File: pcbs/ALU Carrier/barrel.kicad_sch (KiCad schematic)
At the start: 3 parts, among them U6001 74HC14

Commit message: Working towards the connectors
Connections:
- net B3: now also U6001.13; no longer U6001.1
- net B3_inv: now also U6001.12; no longer U6001.2
- net GND: now also U6001.1; no longer U6001.13
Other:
- moved on the sheet: U6001A, U6001F
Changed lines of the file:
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@@
 	(symbol
 		(lib_id "74xx:74HC14")
-		(at 83.82 177.8 0)
+		(at 83.82 114.3 0)
 		(unit 6)
 		(exclude_from_sim no)
@@
 		(fields_autoplaced yes)
 		(property "Reference" "U6001"
-			(at 83.82 168.91 0)
+			(at 83.82 105.41 0)
 			(effects
 				(font
@@
 		)
 		(property "Value" "74HC14"
-			(at 83.82 171.45 0)
+			(at 83.82 107.95 0)
 			(effects
 				(font
@@
 		)
 		(property "Footprint" "Package_SO:SOIC-14_3.9x8.7mm_P1.27mm"
-			(at 83.82 177.8 0)
+			(at 83.82 114.3 0)
 			(effects
 				(font
@@
 		)
 		(property "Datasheet" "https://www.lcsc.com/datasheet/lcsc_datasheet_2407241044_Nexperia-74HC14D-653_C5605.pdf"
-			(at 83.82 177.8 0)
+			(at 83.82 114.3 0)
 			(effects
 				(font
@@
 		)
 		(property "Description" "Hex inverter schmitt trigger"
-			(at 83.82 177.8 0)
+			(at 83.82 114.3 0)
 			(effects
 				(font
@@
 		)
 		(property "LCSC" "C5605"
-			(at 83.82 177.8 0)
+			(at 83.82 114.3 0)
 			(effects
 				(font
@@
 	(symbol
 		(lib_id "74xx:74HC14")
-		(at 83.82 114.3 0)
+		(at 83.82 177.8 0)
 		(unit 1)
 		(exclude_from_sim no)
@@
 		(fields_autoplaced yes)
 		(property "Reference" "U6001"
-			(at 83.82 105.41 0)
+			(at 83.82 168.91 0)
 			(effects
 				(font
@@
 		)
 		(property "Value" "74HC14"
-			(at 83.82 107.95 0)
+			(at 83.82 171.45 0)
 			(effects
 				(font
@@
 		)
 		(property "Footprint" "Package_SO:SOIC-14_3.9x8.7mm_P1.27mm"
-			(at 83.82 114.3 0)
+			(at 83.82 177.8 0)
 			(effects
 				(font
@@
 		)
 		(property "Datasheet" "https://www.lcsc.com/datasheet/lcsc_datasheet_2407241044_Nexperia-74HC14D-653_C5605.pdf"
-			(at 83.82 114.3 0)
+			(at 83.82 177.8 0)
 			(effects
 				(font
@@
 		)
 		(property "Description" "Hex inverter schmitt trigger"
-			(at 83.82 114.3 0)
+			(at 83.82 177.8 0)
 			(effects
 				(font
@@
 		)
 		(property "LCSC" "C5605"
-			(at 83.82 114.3 0)
-			(effects
-				(font
+			(at 83.82 177.8 0)
+			(effects
+				(font

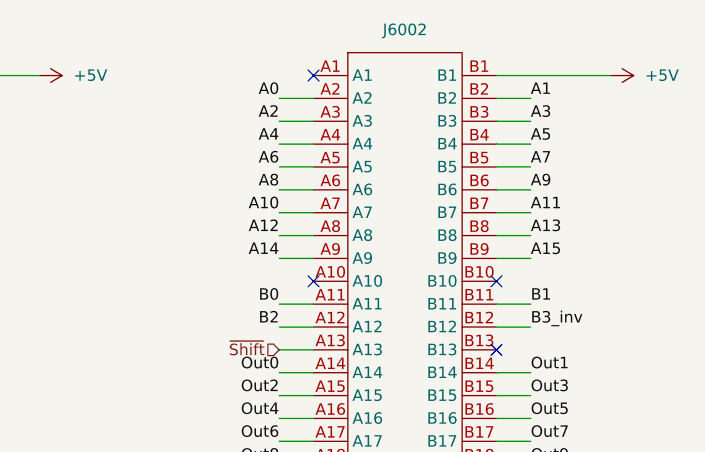
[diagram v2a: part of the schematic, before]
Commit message: Correcting barrel shifter
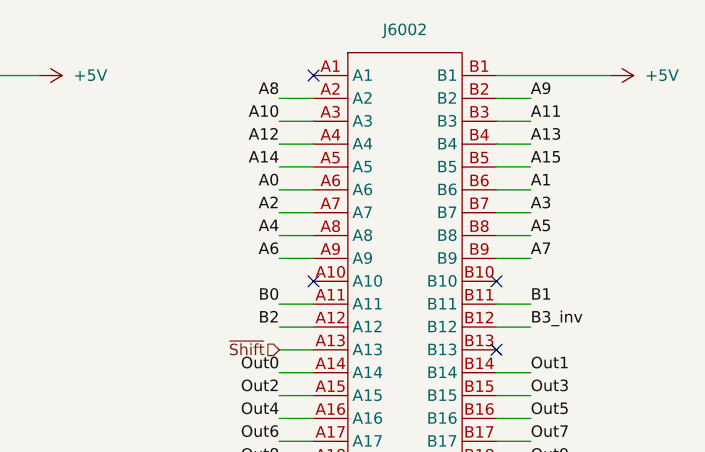
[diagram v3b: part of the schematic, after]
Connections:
- net A0: now also J6002.A6; no longer J6002.A2
- net A1: now also J6002.B6; no longer J6002.B2
- net A10: now also J6002.A3; no longer J6002.A7
- net A11: now also J6002.B3; no longer J6002.B7
- net A12: now also J6002.A4; no longer J6002.A8
- net A13: now also J6002.B4; no longer J6002.B8
- net A14: now also J6002.A5; no longer J6002.A9
- net A15: now also J6002.B5; no longer J6002.B9
- net A2: now also J6002.A7; no longer J6002.A3
- net A3: now also J6002.B7; no longer J6002.B3
- net A4: now also J6002.A8; no longer J6002.A4
- net A5: now also J6002.B8; no longer J6002.B4
- net A6: now also J6002.A9; no longer J6002.A5
- net A7: now also J6002.B9; no longer J6002.B5
- net A8: now also J6002.A2; no longer J6002.A6
- net A9: now also J6002.B2; no longer J6002.B6
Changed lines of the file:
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@@
 	)
 	(label "A4"
-		(at 179.07 43.18 180)
+		(at 179.07 53.34 180)
 		(fields_autoplaced yes)
 		(effects
@@
 	)
 	(label "A10"
-		(at 179.07 50.8 180)
+		(at 179.07 40.64 180)
 		(fields_autoplaced yes)
 		(effects
@@
 	)
 	(label "A11"
-		(at 207.01 50.8 0)
+		(at 207.01 40.64 0)
 		(fields_autoplaced yes)
 		(effects
@@
 	)
 	(label "A2"
-		(at 179.07 40.64 180)
+		(at 179.07 50.8 180)
 		(fields_autoplaced yes)
 		(effects
@@
 	)
 	(label "A8"
-		(at 179.07 48.26 180)
+		(at 179.07 38.1 180)
 		(fields_autoplaced yes)
 		(effects
@@
 	)
 	(label "A6"
-		(at 179.07 45.72 180)
+		(at 179.07 55.88 180)
 		(fields_autoplaced yes)
 		(effects
@@
 	)
 	(label "A0"
-		(at 179.07 38.1 180)
+		(at 179.07 48.26 180)
 		(fields_autoplaced yes)
 		(effects
@@
 	)
 	(label "A7"
-		(at 207.01 45.72 0)
+		(at 207.01 55.88 0)
 		(fields_autoplaced yes)
 		(effects
@@
 	)
 	(label "A3"
-		(at 207.01 40.64 0)
+		(at 207.01 50.8 0)
 		(fields_autoplaced yes)
 		(effects
@@
 	)
 	(label "A12"
-		(at 179.07 53.34 180)
+		(at 179.07 43.18 180)
 		(fields_autoplaced yes)
 		(effects
@@
 	)
 	(label "A5"
-		(at 207.01 43.18 0)
+		(at 207.01 53.34 0)
 		(fields_autoplaced yes)
 		(effects
@@
 	)
 	(label "A14"
-		(at 179.07 55.88 180)
+		(at 179.07 45.72 180)
 		(fields_autoplaced yes)
 		(effects
@@
 	)
 	(label "A15"
-		(at 207.01 55.88 0)
+		(at 207.01 45.72 0)
 		(fields_autoplaced yes)
 		(effects
@@
 	)
 	(label "A1"
-		(at 207.01 38.1 0)
+		(at 207.01 48.26 0)
 		(fields_autoplaced yes)
 		(effects
@@
 	)
 	(label "A9"
-		(at 207.01 48.26 0)
+		(at 207.01 38.1 0)
 		(fields_autoplaced yes)
 		(effects
@@
 	)
 	(label "A13"
-		(at 207.01 53.34 0)
-		(fields_autoplaced yes)
-		(effects
+		(at 207.01 43.18 0)
+		(fields_autoplaced yes)
+		(effects
